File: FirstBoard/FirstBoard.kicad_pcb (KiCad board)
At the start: 2 copper layers, 25 parts, among them J0 Battery, J1 MPU0, J10 MPU9, J11 MPU10, J12 MPU11, J13 MPU12, J14 OPEN, J2 MPU1, J3 MPU2, J4 MPU3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

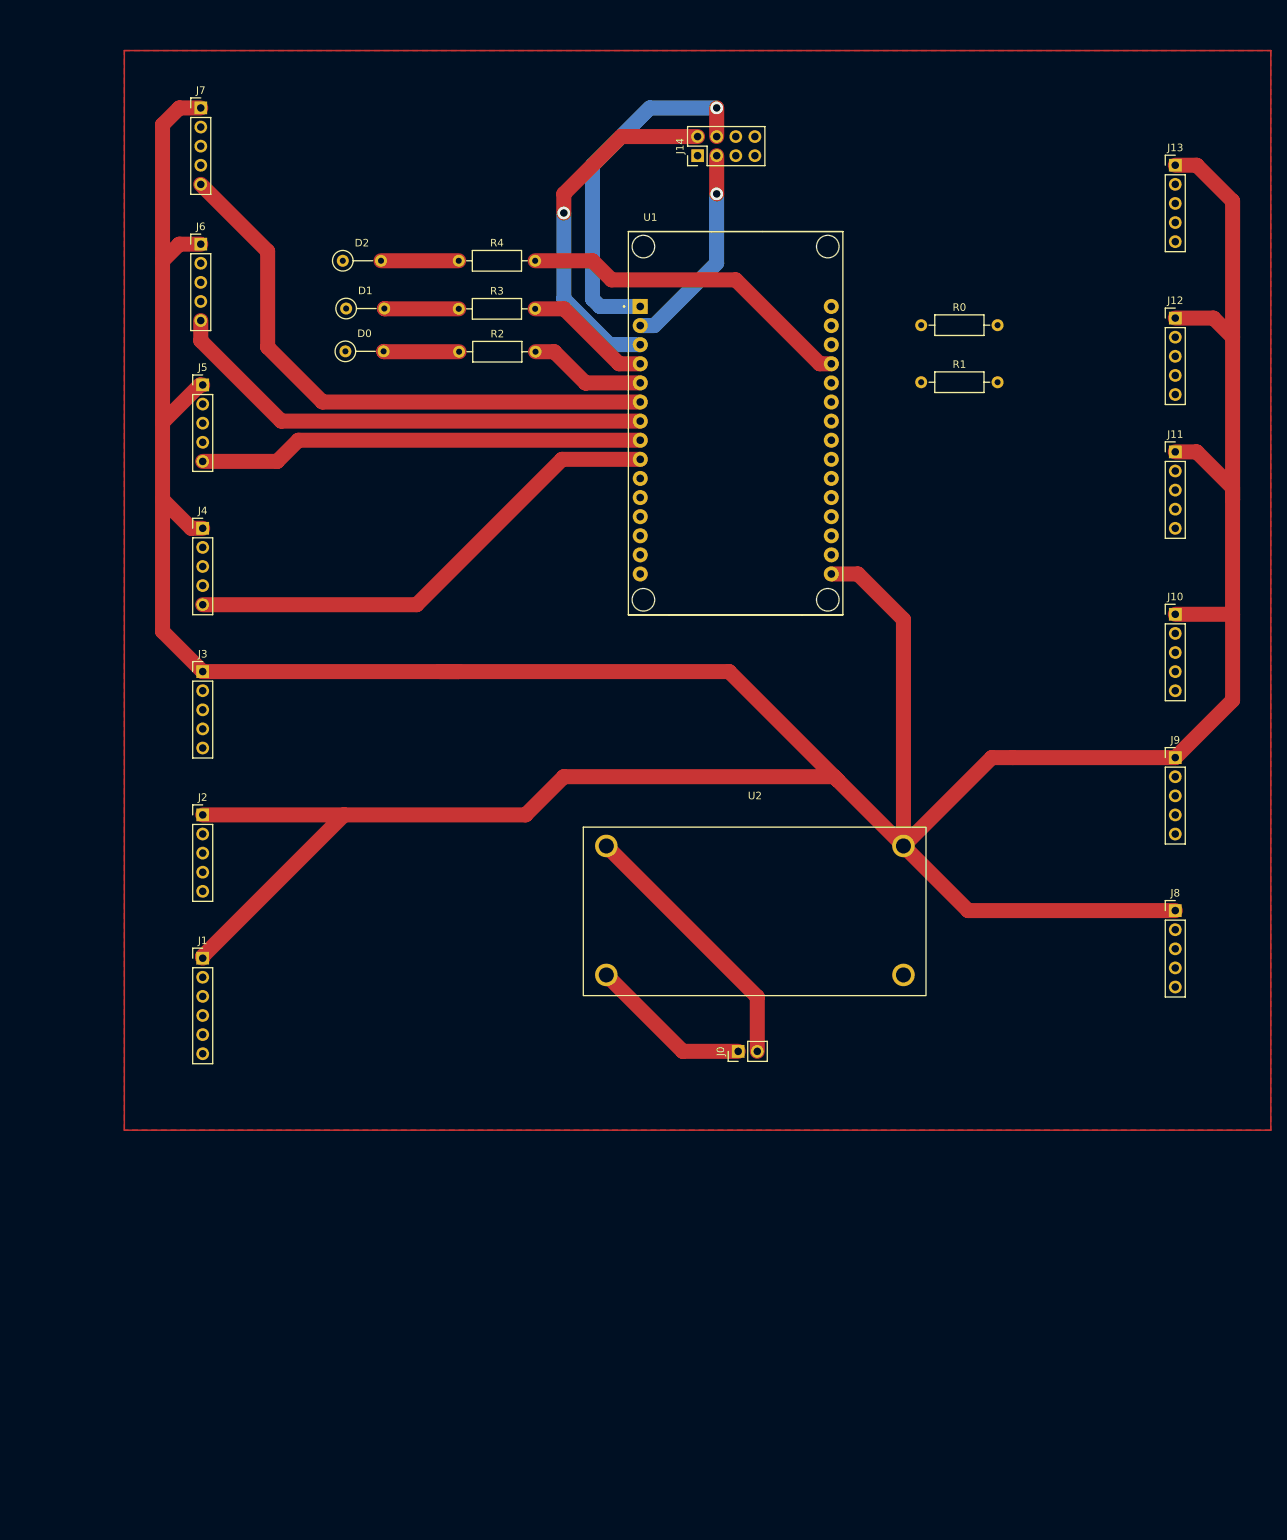
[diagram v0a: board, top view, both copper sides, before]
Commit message: changing layour, adding SD card
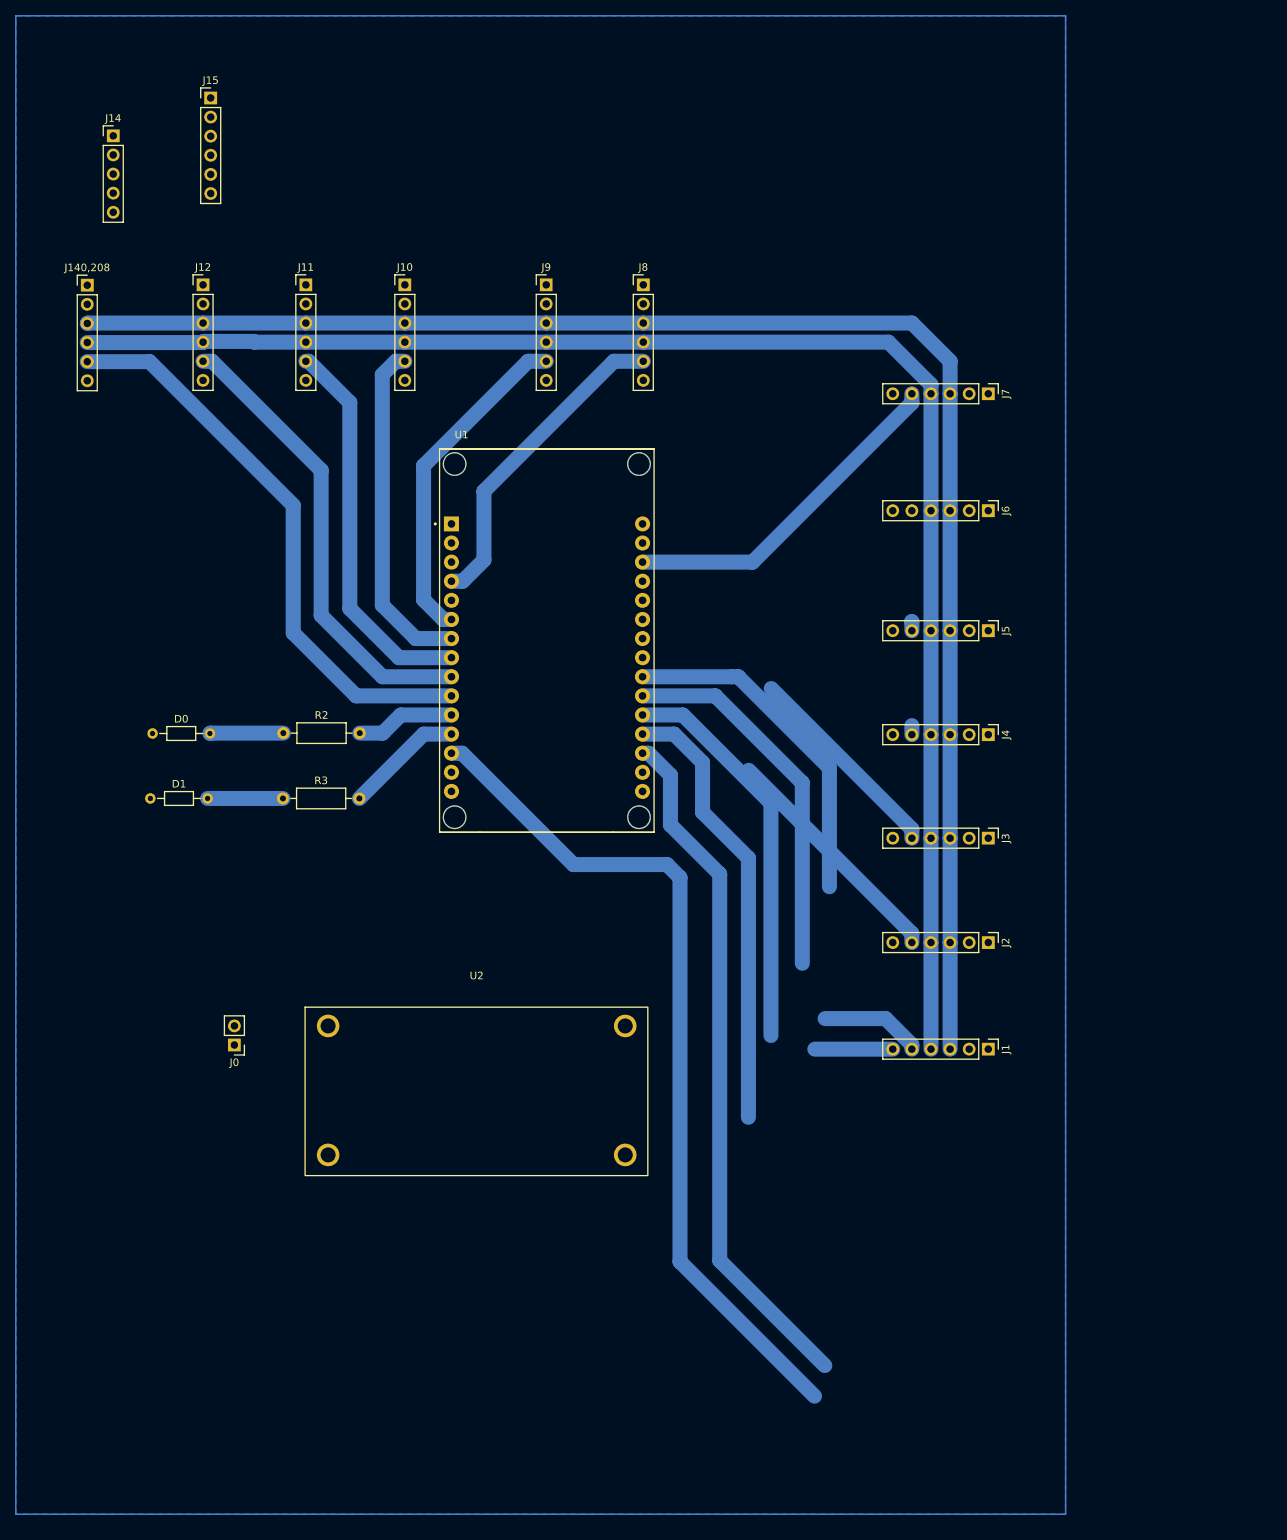
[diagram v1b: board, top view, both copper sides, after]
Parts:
- removed D2: LED B, Resistor_THT:R_Axial_DIN0207_L6.3mm_D2.5mm_P5.08mm_Vertical
- removed J13: MPU12, Connector_PinHeader_2.54mm:PinHeader_1x05_P2.54mm_Vertical
- removed R0, R1: 4k7, Resistor_THT:R_Axial_DIN0207_L6.3mm_D2.5mm_P10.16mm_Horizontal
- removed R4: 220R, Resistor_THT:R_Axial_DIN0207_L6.3mm_D2.5mm_P10.16mm_Horizontal
- added J140,208: MPU12, Connector_PinHeader_2.54mm:PinHeader_1x06_P2.54mm_Vertical, F.Cu at (20.5, 43.9)
- added J15: SD_CARD, Connector_PinHeader_2.54mm:PinHeader_1x06_P2.54mm_Vertical, F.Cu at (36.9, 19.0)
- D0, D1: footprint Resistor_THT:R_Axial_DIN0207_L6.3mm_D2.5mm_P5.08mm_Vertical -> Resistor_THT:R_Axial_DIN0204_L3.6mm_D1.6mm_P7.62mm_Horizontal
- J10, J11, J12, J2, J4, J5, J6, J7, J8, J9: footprint Connector_PinHeader_2.54mm:PinHeader_1x05_P2.54mm_Vertical -> Connector_PinHeader_2.54mm:PinHeader_1x06_P2.54mm_Vertical
- J14: value OPEN -> Open; footprint Connector_PinHeader_2.54mm:PinHeader_2x04_P2.54mm_Vertical -> Connector_PinHeader_2.54mm:PinHeader_1x05_P2.54mm_Vertical
- J3: value MPU2 -> MPU3; footprint Connector_PinHeader_2.54mm:PinHeader_1x05_P2.54mm_Vertical -> Connector_PinHeader_2.54mm:PinHeader_1x06_P2.54mm_Vertical
- moved J12 129.3 mm to (35.9, 43.8)
- moved J11 117.7 mm to (49.5, 43.8)
- moved J10 111.4 mm to (62.7, 43.8)
- moved J7 111.4 mm to (140.2, 58.3), turned to -90 degrees
- moved J6 110.5 mm to (140.2, 73.9), turned to -90 degrees
- moved J5 109.4 mm to (140.2, 89.8), turned to -90 degrees
- moved J8 109.2 mm to (94.4, 43.8)
- moved J4 108.0 mm to (140.2, 103.6), turned to -90 degrees
- moved J3 106.8 mm to (140.2, 117.4), turned to -90 degrees
- moved J2 105.8 mm to (140.2, 131.3), turned to -90 degrees
- moved J1 105.1 mm to (140.2, 145.4), turned to -90 degrees
- moved J9 104.6 mm to (81.5, 43.8)
- moved J14 77.7 mm to (23.9, 24.0), turned to 0 degrees
- moved D1 70.1 mm to (28.9, 112.1)
- moved R3 69.2 mm to (46.5, 112.1)
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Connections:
- J1 pad 3: SDA -> SCL
- J1 pad 4: SCL -> SDA
- J10 pad 3: SDA -> SCL
- J10 pad 4: SCL -> SDA
- J11 pad 3: SDA -> SCL
- J11 pad 4: SCL -> SDA
- J12 pad 3: SDA -> SCL
- J12 pad 4: SCL -> SDA
- J14 pad 5: SCK -> Net-(J14-Pad5)
- J2 pad 3: SDA -> SCL
- J2 pad 4: SCL -> SDA
- J3 pad 3: SDA -> SCL
- J3 pad 4: SCL -> SDA
- J4 pad 3: SDA -> SCL
- J4 pad 4: SCL -> SDA
- J5 pad 3: SDA -> SCL
- J5 pad 4: SCL -> SDA
- J6 pad 3: SDA -> SCL
- J6 pad 4: SCL -> SDA
- J7 pad 3: SDA -> SCL
- J7 pad 4: SCL -> SDA
- J8 pad 3: SDA -> SCL
- J8 pad 4: SCL -> SDA
- J9 pad 3: SDA -> SCL
- J9 pad 4: SCL -> SDA
- U1 pad 1: Net-(J14-Pad4) -> Net-(J14-Pad5)
- U1 pad 10: AD0_2 -> AD0_12
- U1 pad 11: AD0_1 -> LED_R
- U1 pad 12: AD0_0 -> LED_G
- U1 pad 18: AD0_7 -> AD0_0
- U1 pad 19: AD0_8 -> AD0_1
- U1 pad 2: Net-(J14-Pad3) -> Net-(J14-Pad4)
- U1 pad 20: AD0_9 -> AD0_2
- U1 pad 21: AD0_10 -> AD0_3
- U1 pad 22: AD0_11 -> AD0_4
- U1 pad 23: AD0_12 -> SS
- U1 pad 27: LED_B -> AD0_5
- U1 pad 28: D1 -> AD0_6
- U1 pad 3: Net-(J14-Pad2) -> Net-(J14-Pad3)
- U1 pad 4: LED_G -> AD0_7
- U1 pad 5: LED_R -> Net-(J14-Pad2)
- U1 pad 6: AD0_6 -> AD0_8
- U1 pad 7: AD0_5 -> AD0_9
- U1 pad 8: AD0_4 -> AD0_10
- U1 pad 9: AD0_3 -> AD0_11
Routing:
- net 3v3: track 557.1 -> 0.00 mm
- net SCL: track 0.00 -> 208.3 mm
- net SDA: track 0.00 -> 202.9 mm
- net INT: track 0.00 -> 123.9 mm
- net AD0_0: track 0.00 -> 105.5 mm
- net AD0_1: track 0.00 -> 91.1 mm
- net AD0_2: track 0.00 -> 80.5 mm
- net AD0_12: track 0.00 -> 76.8 mm
- net AD0_5: track 65.5 -> 0.00 mm
- net AD0_11: track 0.00 -> 61.7 mm
- net AD0_10: track 0.00 -> 51.7 mm
- net Net-(J14-Pad4): track 48.0 -> 0.00 mm, vias 1 -> 0
- net Net-(J14-Pad2): track 47.6 -> 0.00 mm, vias 1 -> 0
- net AD0_9: track 0.00 -> 45.4 mm
- net LED_B: track 45.0 -> 0.00 mm
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- added copper zone on B.Cu, net GND
- removed copper zone on F.Cu, net GND

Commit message: First version -SD Card+13 IMUs
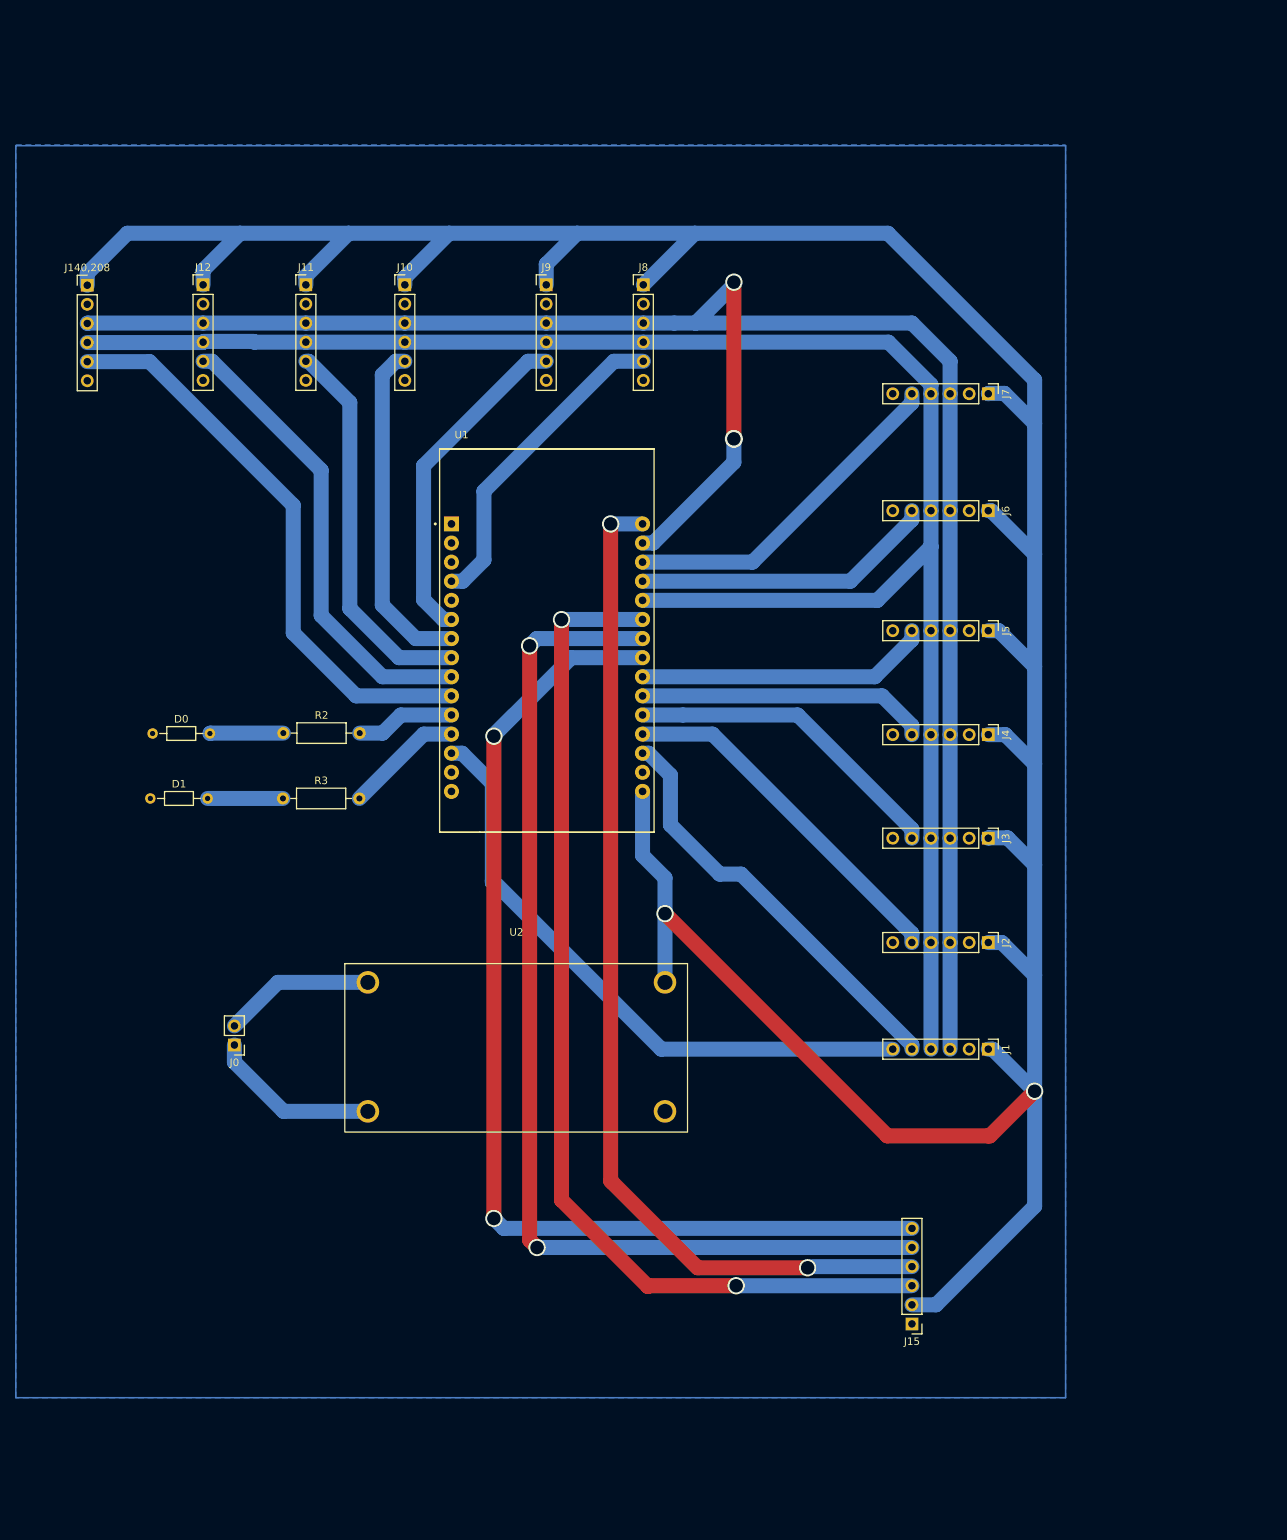
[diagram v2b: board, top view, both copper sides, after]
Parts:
- removed J14: Open, Connector_PinHeader_2.54mm:PinHeader_1x05_P2.54mm_Vertical
- moved J15 187.7 mm to (130.1, 182.0), turned to 180 degrees
- moved U2 7.84 mm to (77.5, 145.1)
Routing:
- net 3v3: track 0.00 -> 461.9 mm, vias 0 -> 2
- net SS: track 0.00 -> 148.1 mm, vias 0 -> 2
- net SCK: track 0.00 -> 145.6 mm, vias 0 -> 2
- net MISO: track 0.00 -> 139.4 mm, vias 0 -> 2
- net MOSI: track 0.00 -> 135.7 mm, vias 0 -> 2
- net AD0_0: track 105.5 -> 56.3 mm
- net SCL: track 208.3 -> 256.5 mm, vias 0 -> 2
- net AD0_1: track 91.1 -> 48.0 mm
- net SDA: track 202.9 -> 244.2 mm
- net INT: track 123.9 -> 83.0 mm
- net AD0_5: track 0.00 -> 40.4 mm
- net AD0_2: track 80.5 -> 43.3 mm
- net BAT-: track 0.00 -> 22.7 mm
- net BAT+: track 0.00 -> 20.1 mm
- net AD0_3: track 51.2 -> 38.6 mm
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
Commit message: Bigger space and vias
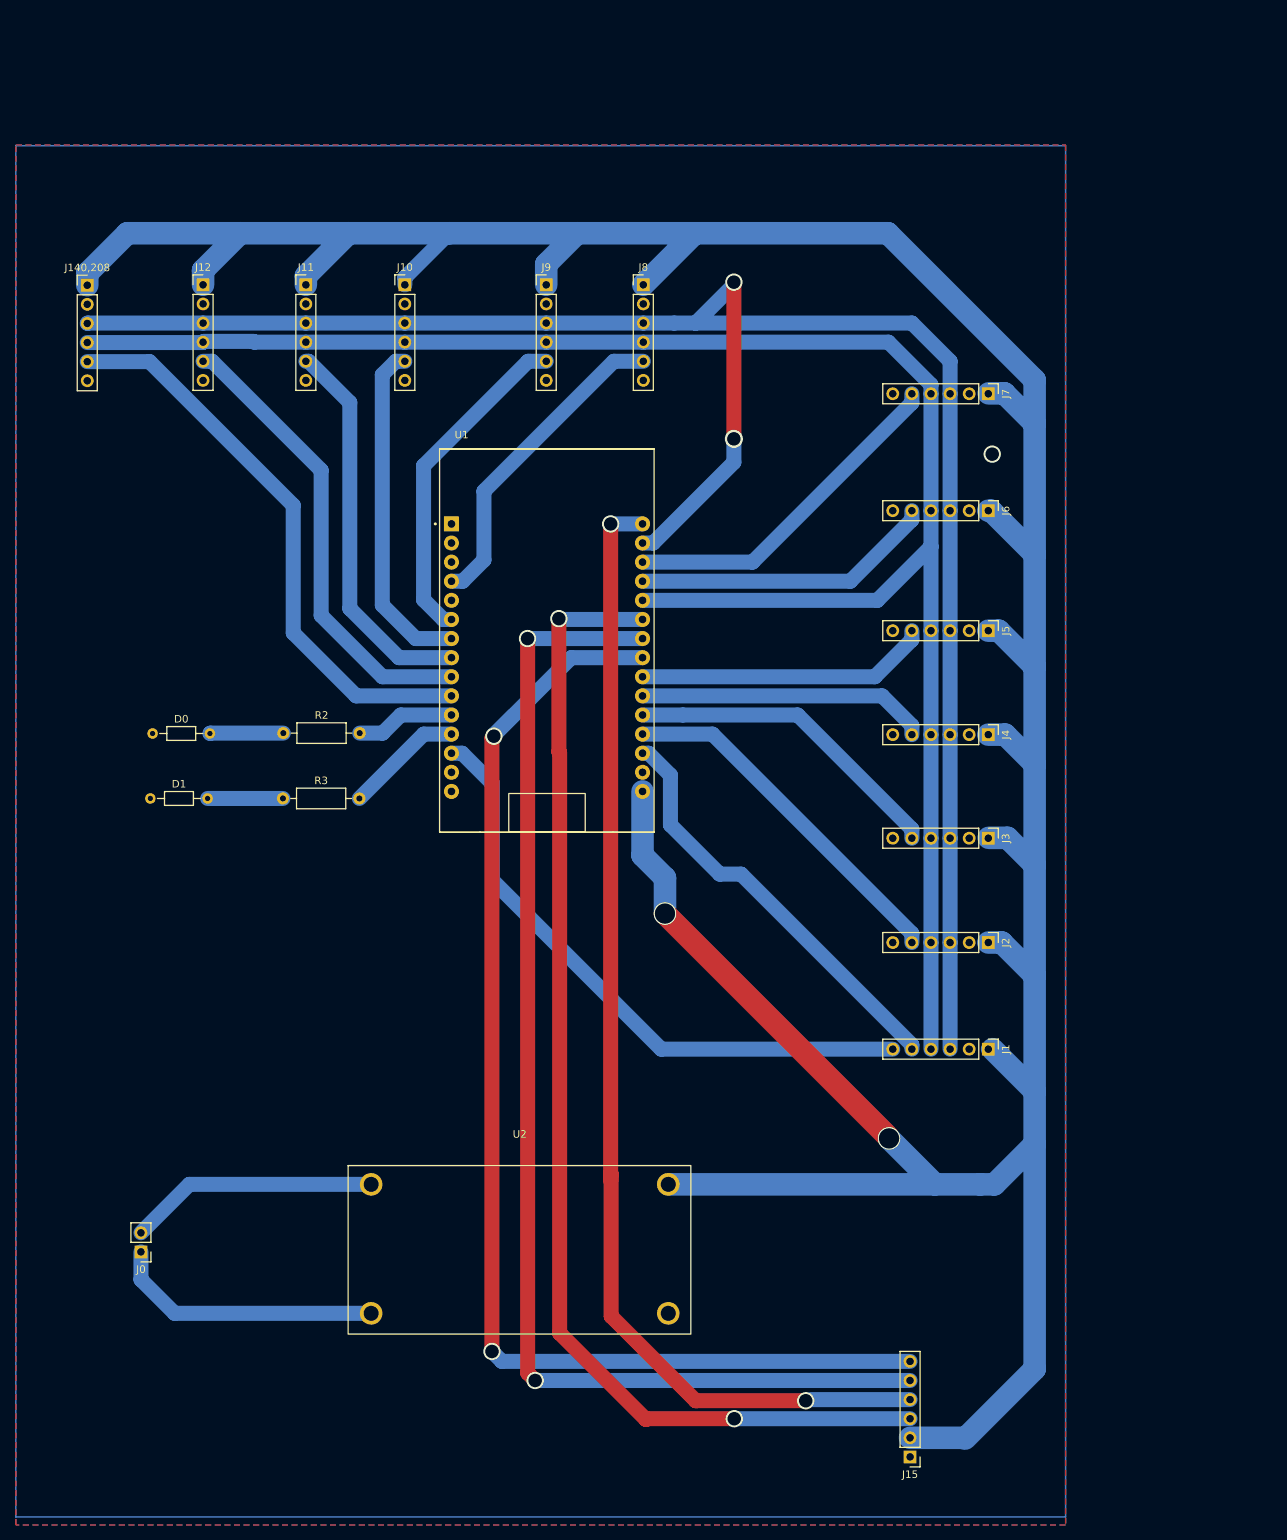
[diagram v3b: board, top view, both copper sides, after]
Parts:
- moved J0 30.2 mm to (27.6, 172.4)
- moved U2 26.9 mm to (78.0, 172.0)
- moved J15 17.7 mm to (129.8, 199.6)
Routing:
- net 3v3: track 461.9 -> 516.6 mm
- net SCK: track 145.6 -> 164.2 mm
- net MOSI: track 135.7 -> 154.3 mm
- net MISO: track 139.4 -> 157.6 mm
- net SS: track 148.1 -> 165.9 mm
- net BAT-: track 22.7 -> 36.1 mm
- net BAT+: track 20.1 -> 33.3 mm
- net INT: track 83.0 -> 82.5 mm
- net GND: vias 0 -> 1
- added copper zone on F.Cu, net GND
